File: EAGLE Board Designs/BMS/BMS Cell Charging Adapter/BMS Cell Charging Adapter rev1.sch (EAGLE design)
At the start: 21 parts, among them X1 CONNECTOR-10, X2 CONNECTOR-10

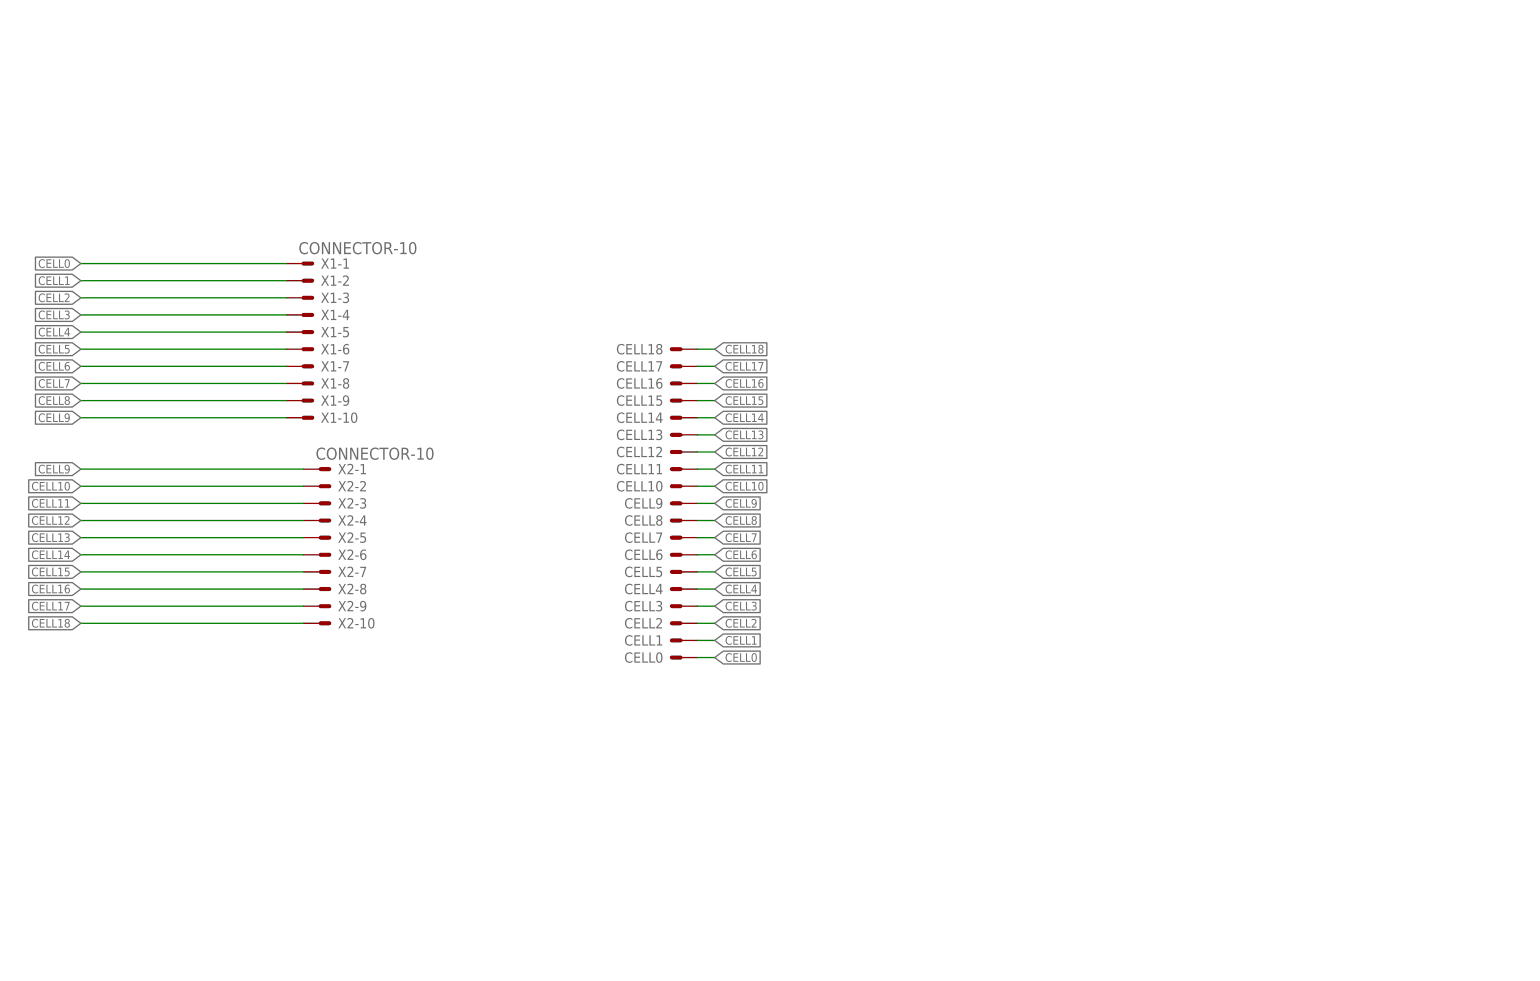
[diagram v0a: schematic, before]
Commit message: added a frame to the schematic
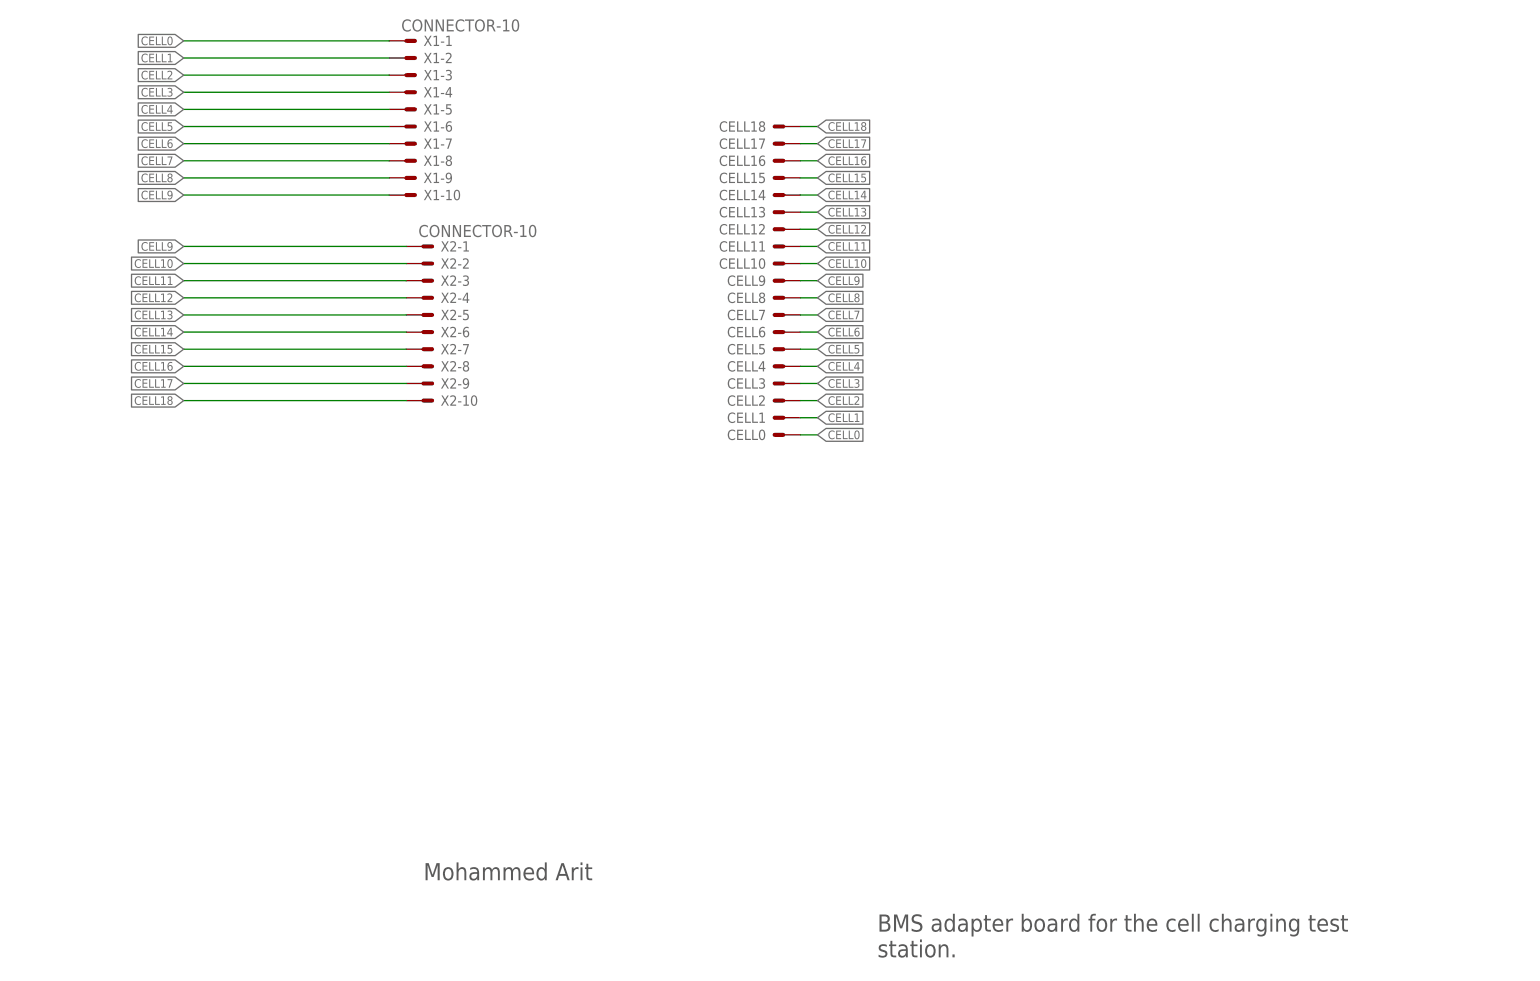
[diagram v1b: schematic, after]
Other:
- note added: "BMS adapter board for the cell charging test station."
- note added: "Mohammed Arit"
- moved on the sheet: CELL0, CELL1, CELL10, CELL11, CELL12, CELL13, CELL14, CELL15, CELL16, CELL17, CELL18, CELL2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
